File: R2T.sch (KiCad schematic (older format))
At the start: 10 parts, among them J1 12V_Input, J2 Conn_02x01, J3 Conn_01x07, J4 Conn_01x07, U0 μA78Lxx, U1 Teensy3.5

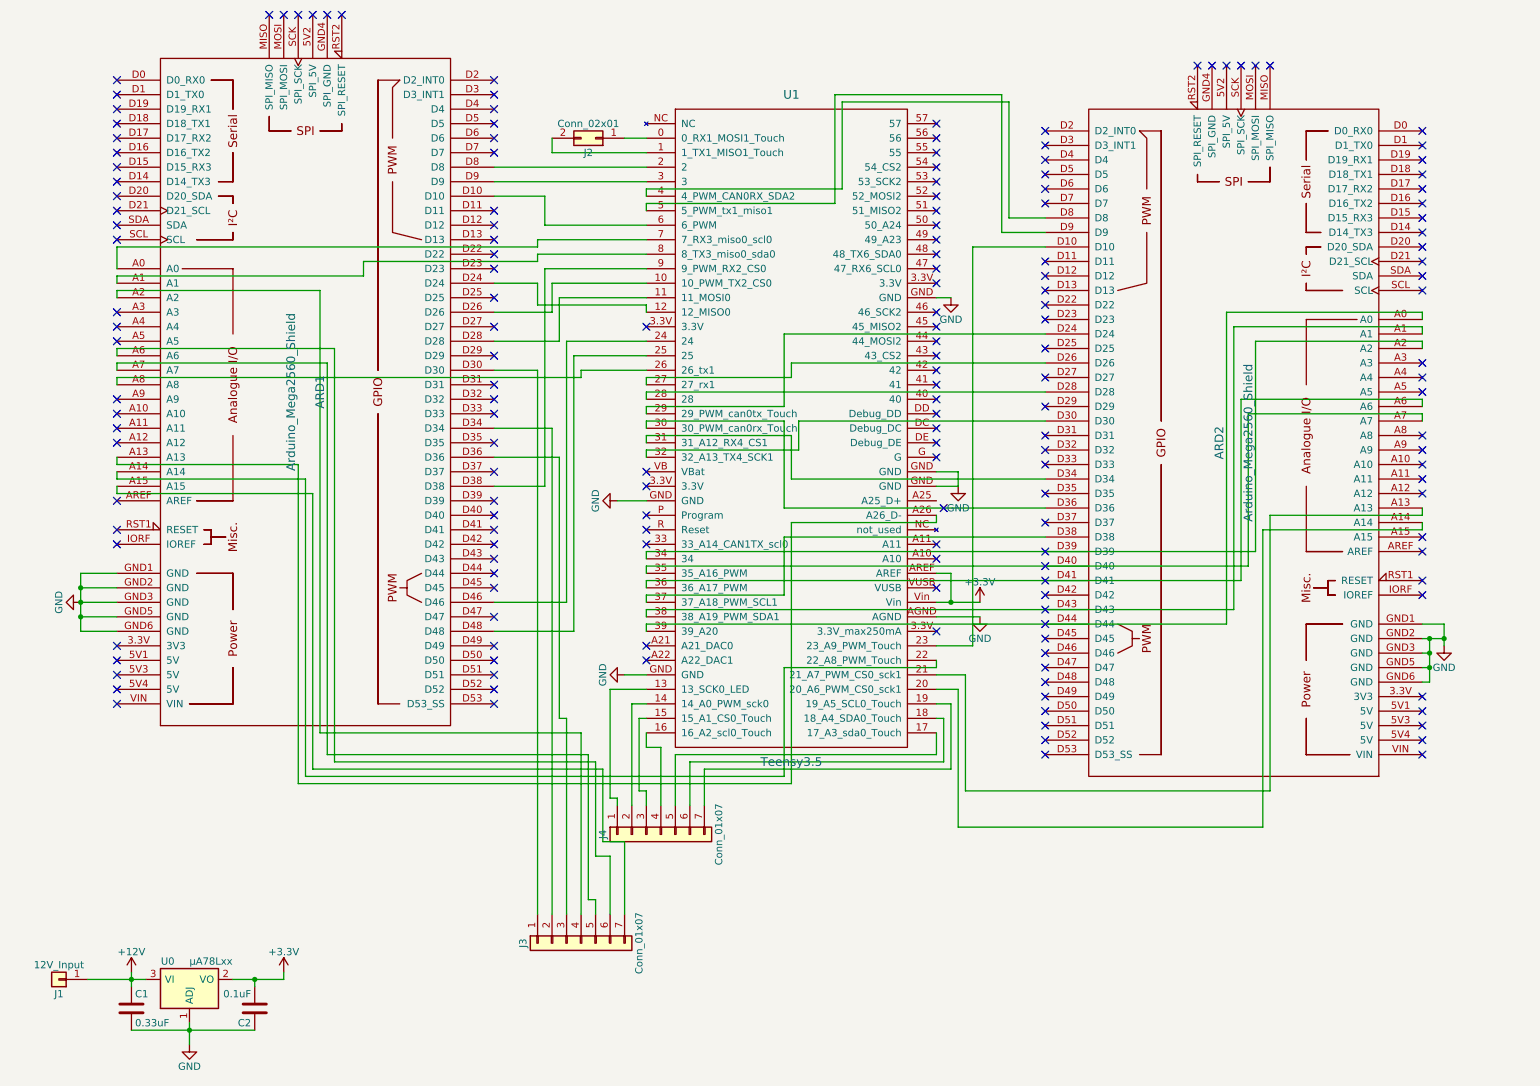
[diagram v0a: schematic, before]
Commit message: Added a 3rd pin on the connector for the serial debug on the teensy : gnd added
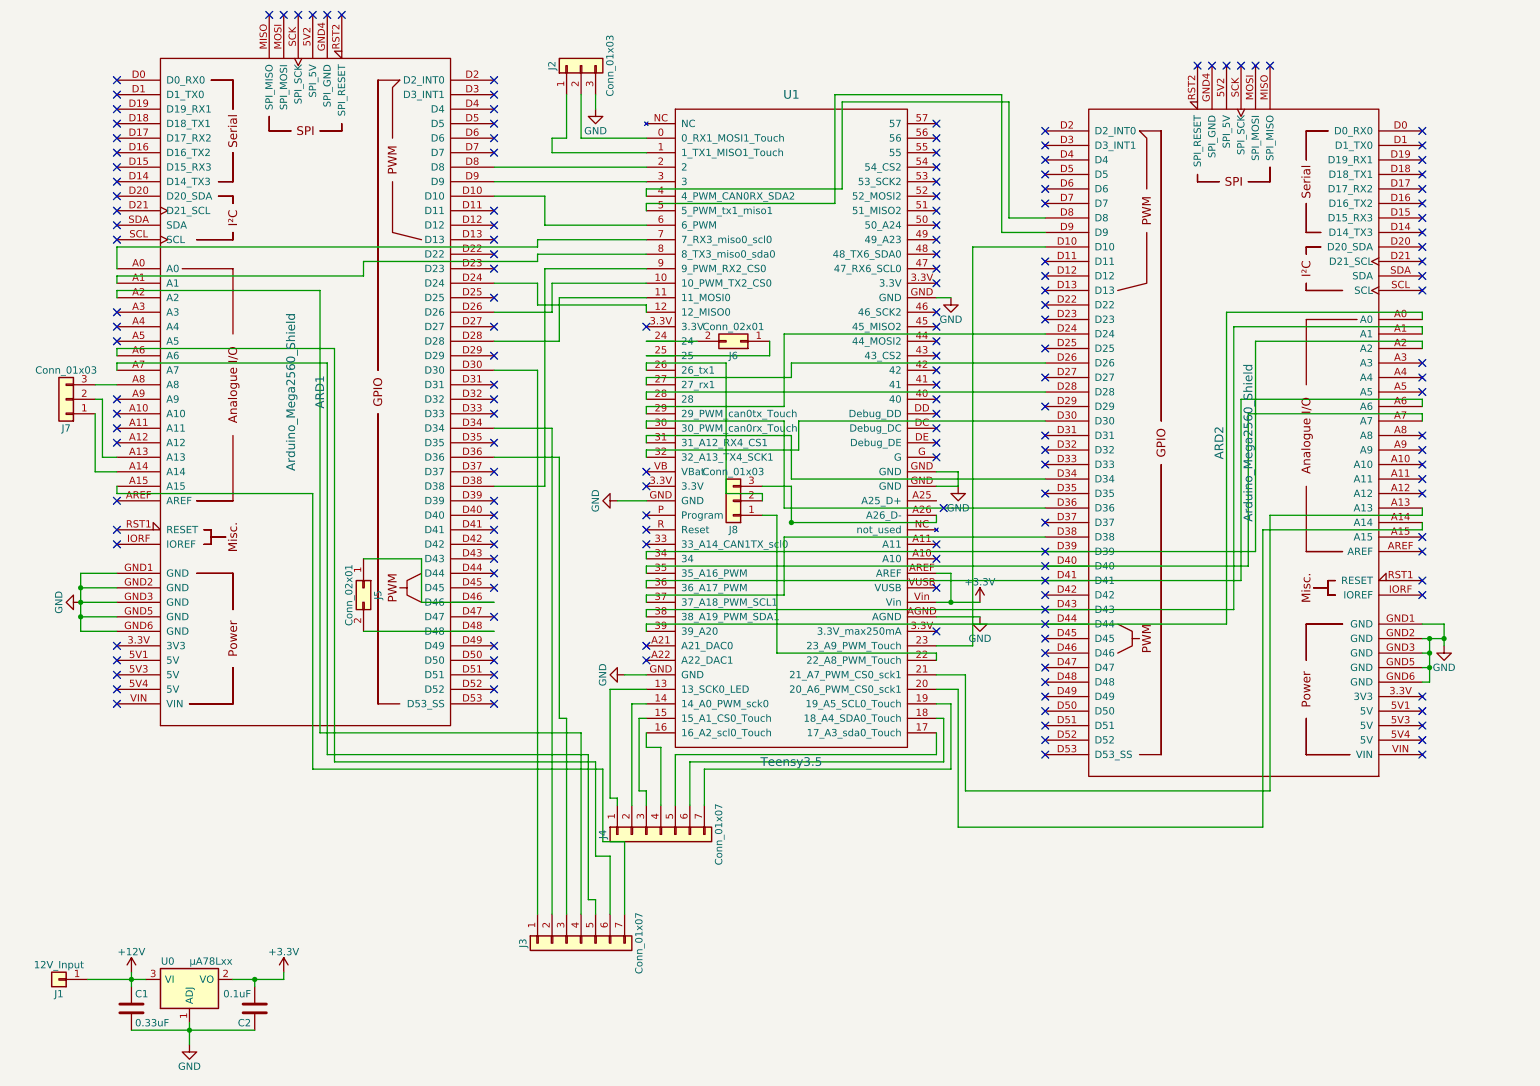
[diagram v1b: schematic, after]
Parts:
- removed J2: Conn_02x01, Connector_PinSocket_2.00mm:PinSocket_1x02_P2.00mm_Horizontal, symbol Conn_02x01
- added J2, J7, J8: Conn_01x03, Connector_PinHeader_2.00mm:PinHeader_1x03_P2.00mm_Vertical, symbol Conn_01x03
- added J5, J6: Conn_02x01, Connector_PinSocket_2.00mm:PinSocket_1x02_P2.00mm_Horizontal, symbol Conn_02x01
- J3, J4: footprint Connector_PinSocket_2.54mm:PinSocket_1x07_P2.54mm_Vertical -> Connector_PinHeader_2.00mm:PinHeader_1x07_P2.00mm_Vertical
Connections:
- net GND: now also J2.3 (Pin_3)
- net at U1.0 (0_RX1_MOSI1_Touch): now also J2.2 (Pin_2)
- net at U1.1 (1_TX1_MISO1_Touch): now also J2.1 (Pin_1)
- net at U1.22 (22_A8_PWM_Touch): now also J8.1 (Pin_1); no longer ARD1.A14
- net at U1.24: now also J6.2 (Pin_2); no longer ARD1.D46
- net at U1.25: now also J6.1 (Pin_1); no longer ARD1.D48
- net at U1.26 (26_tx1): now also J8.2 (Pin_2); no longer ARD1.A8
- net at U1.A26 (A26_D-): now also J8.3 (Pin_3); no longer ARD1.A13
- new net: ARD1.A13, J7.2 (Pin_2)
- new net: ARD1.A14, J7.1 (Pin_1)
- new net: ARD1.A8, J7.3 (Pin_3)
- new net: ARD1.D46, J5.1 (Pin_1)
- new net: ARD1.D48, J5.2 (Pin_2)
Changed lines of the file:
@@
 NoConn ~ 4750 3550
 NoConn ~ 4750 2550
-$Comp
-L Conn_02x01 J2
-U 1 1 5A55909C
-P 4400 1250
-F 0 "J2" H 4450 1350 50  0000 C CNN
-F 1 "Conn_02x01" H 4450 1150 50  0000 C CNN
-F 2 "Connector_PinSocket_2.00mm:PinSocket_1x02_P2.00mm_Horizontal" H 4400 1250 50  0001 C CNN
-F 3 "" H 4400 1250 50  0001 C CNN
-	1    4400 1250
-	-1   0    0    1
-$EndComp
 NoConn ~ 7500 4300
 NoConn ~ 7500 4200
@@
 	1100 3700 1100 3650
 Wire Wire Line
-	1100 3550 1100 3600
-Wire Wire Line
-	1100 3600 2400 3600
-Wire Wire Line
-	2400 3600 2400 5650
-Wire Wire Line
-	2400 5650 5700 5650
-Wire Wire Line
-	5700 5650 5700 4900
-Wire Wire Line
-	5700 4900 6750 4900
-Wire Wire Line
-	6750 4900 6750 4850
-Wire Wire Line
-	4750 2650 4200 2650
-Wire Wire Line
-	4200 2650 4200 4450
-Wire Wire Line
-	4200 4450 3700 4450
-Wire Wire Line
-	4750 2750 4250 2750
-Wire Wire Line
-	4250 2750 4250 4650
-Wire Wire Line
-	4250 4650 3700 4650
-Wire Wire Line
-	1100 2950 1100 2900
-Wire Wire Line
-	1100 2900 4300 2900
-Wire Wire Line
-	4300 2900 4300 2850
-Wire Wire Line
-	4300 2850 4750 2850
-Wire Wire Line
-	1100 3450 1100 3500
-Wire Wire Line
-	1100 3500 2350 3500
-Wire Wire Line
-	2350 3500 2350 5700
-Wire Wire Line
-	2350 5700 5750 5700
-Wire Wire Line
-	5750 5700 5750 3900
-Wire Wire Line
 	5750 3900 6750 3900
 Wire Wire Line
@@
 	6850 2350 6750 2350
 Wire Wire Line
-	4750 1250 4600 1250
+	4300 1250 4750 1250
 Wire Wire Line
 	4750 1350 4100 1350
@@
 F 0 "J4" H 4850 6450 50  0000 C CNN
 F 1 "Conn_01x07" H 4850 5650 50  0000 C CNN
-F 2 "Connector_PinSocket_2.54mm:PinSocket_1x07_P2.54mm_Vertical" H 4850 6050 50  0001 C CNN
+F 2 "Connector_PinHeader_2.00mm:PinHeader_1x07_P2.00mm_Vertical" H 4850 6050 50  0001 C CNN
 F 3 "" H 4850 6050 50  0001 C CNN
 	1    4850 6050
@@
 F 0 "J3" H 4300 7200 50  0000 C CNN
 F 1 "Conn_01x07" H 4300 6400 50  0000 C CNN
-F 2 "Connector_PinSocket_2.54mm:PinSocket_1x07_P2.54mm_Vertical" H 4300 6800 50  0001 C CNN
+F 2 "Connector_PinHeader_2.00mm:PinHeader_1x07_P2.00mm_Vertical" H 4300 6800 50  0001 C CNN
 F 3 "" H 4300 6800 50  0001 C CNN
 	1    4300 6800
@@
 Wire Wire Line
 	4400 6500 4400 6600
+$Comp
+L Conn_02x01 J5
+U 1 1 5A5645DD
+P 2800 4350
+F 0 "J5" H 2850 4450 50  0000 C CNN
+F 1 "Conn_02x01" H 2850 4250 50  0000 C CNN
+F 2 "Connector_PinSocket_2.00mm:PinSocket_1x02_P2.00mm_Horizontal" H 2800 4350 50  0001 C CNN
+F 3 "" H 2800 4350 50  0001 C CNN
+	1    2800 4350
+	0    1    1    0
+$EndComp
+Wire Wire Line
+	3200 4450 3200 4150
+Wire Wire Line
+	3200 4150 2800 4150
+$Comp
+L Conn_02x01 J6
+U 1 1 5A5648FB
+P 5400 2650
+F 0 "J6" H 5450 2750 50  0000 C CNN
+F 1 "Conn_02x01" H 5450 2550 50  0000 C CNN
+F 2 "Connector_PinSocket_2.00mm:PinSocket_1x02_P2.00mm_Horizontal" H 5400 2650 50  0001 C CNN
+F 3 "" H 5400 2650 50  0001 C CNN
+	1    5400 2650
+	-1   0    0    1
+$EndComp
+Wire Wire Line
+	5600 2750 5600 2650
+Wire Wire Line
+	3700 4650 2800 4650
+Wire Wire Line
+	3700 4450 3200 4450
+Wire Wire Line
+	5100 2650 4750 2650
+Wire Wire Line
+	4750 2750 5600 2750
+$Comp
+L Conn_01x03 J7
+U 1 1 5A565122
+P 750 3050
+F 0 "J7" H 750 3250 50  0000 C CNN
+F 1 "Conn_01x03" H 750 2850 50  0000 C CNN
+F 2 "Connector_PinHeader_2.00mm:PinHeader_1x03_P2.00mm_Vertical" H 750 3050 50  0001 C CNN
+F 3 "" H 750 3050 50  0001 C CNN
+	1    750  3050
+	-1   0    0    1
+$EndComp
+Wire Wire Line
+	1100 2950 950  2950
+Wire Wire Line
+	1100 3450 1000 3450
+Wire Wire Line
+	1000 3450 1000 3050
+Wire Wire Line
+	1000 3050 950  3050
+Wire Wire Line
+	950  3150 950  3550
+Wire Wire Line
+	950  3550 1100 3550
+$Comp
+L Conn_01x03 J8
+U 1 1 5A56593C
+P 5350 3750
+F 0 "J8" H 5350 3950 50  0000 C CNN
+F 1 "Conn_01x03" H 5350 3550 50  0000 C CNN
+F 2 "Connector_PinHeader_2.00mm:PinHeader_1x03_P2.00mm_Vertical" H 5350 3750 50  0001 C CNN
+F 3 "" H 5350 3750 50  0001 C CNN
+	1    5350 3750
+	-1   0    0    1
+$EndComp
+Wire Wire Line
+	6750 4800 5650 4800
+Wire Wire Line
+	5650 4800 5650 3850
+Wire Wire Line
+	5650 3850 5550 3850
+Wire Wire Line
+	5550 3750 5550 3700
+Wire Wire Line
+	5550 3700 5300 3700
+Wire Wire Line
+	5300 3700 5300 2800
+Wire Wire Line
+	5300 2800 4750 2800
+Wire Wire Line
+	4750 2800 4750 2850
+Wire Wire Line
+	5550 3650 5750 3650
+Connection ~ 5750 3900
+Wire Wire Line
+	5750 3650 5750 3900
+Wire Wire Line
+	6750 4850 6750 4800
+$Comp
+L Conn_01x03 J2
+U 1 1 5A58CBAA
+P 4300 750
+F 0 "J2" H 4300 950 50  0000 C CNN
+F 1 "Conn_01x03" H 4300 550 50  0000 C CNN
+F 2 "Connector_PinHeader_2.00mm:PinHeader_1x03_P2.00mm_Vertical" H 4300 750 50  0001 C CNN
+F 3 "" H 4300 750 50  0001 C CNN
+	1    4300 750
+	0    -1   -1   0
+$EndComp
+Wire Wire Line
+	4200 950  4200 1250
+Wire Wire Line
+	4200 1250 4100 1250
+Wire Wire Line
+	4300 950  4300 1250
+$Comp
+L GND #PWR012
+U 1 1 5A58CF2A
+P 4400 1050
+F 0 "#PWR012" H 4400 800 50  0001 C CNN
+F 1 "GND" H 4400 900 50  0000 C CNN
+F 2 "" H 4400 1050 50  0001 C CNN
+F 3 "" H 4400 1050 50  0001 C CNN
+	1    4400 1050
+	1    0    0    -1
+$EndComp
+Wire Wire Line
+	4400 950  4400 1050
 $EndSCHEMATC

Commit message: Finished seperating circuits on to 3 diffrent boards : teensy / ramps 0 / ramps 1. Sill need to clean and optimis for space and soder
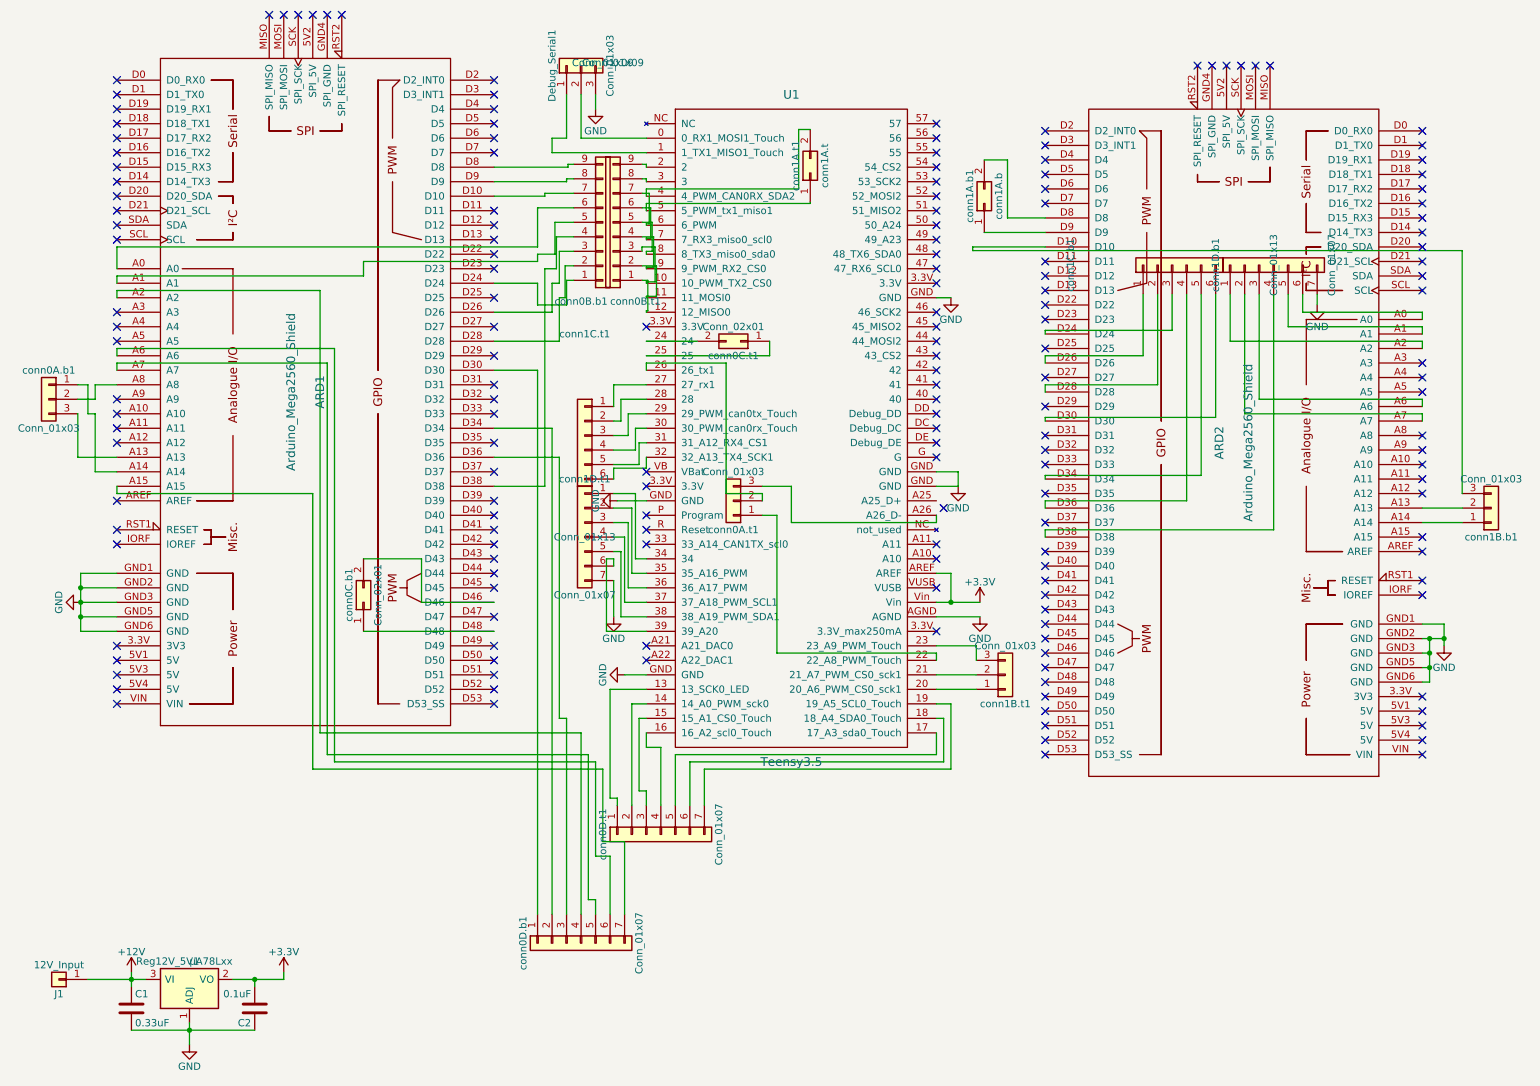
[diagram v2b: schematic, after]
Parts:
- added conn0B.b1, conn0B.t1: Conn_01x09, Connector_PinHeader_2.00mm:PinHeader_1x09_P2.00mm_Vertical, symbol Conn_01x09
- added conn1A.b1: conn1A.b, Connector_PinSocket_2.00mm:PinSocket_2x01_P2.00mm_Vertical, symbol Conn_02x01
- added conn1A.t1: conn1A.t, Connector_PinSocket_2.00mm:PinSocket_2x01_P2.00mm_Vertical, symbol Conn_02x01
- added conn1B.b1, conn1B.t1: Conn_01x03, Connector_PinSocket_2.00mm:PinSocket_1x03_P2.00mm_Vertical, symbol Conn_01x03
- added conn1C.b1, conn1C.t1: Conn_01x13, Connector_PinSocket_2.00mm:PinSocket_1x06_P2.00mm_Vertical, symbol Conn_01x06
- added conn1D.b1, conn1D.t1: Conn_01x07, Connector_PinHeader_2.00mm:PinHeader_1x07_P2.00mm_Vertical, symbol Conn_01x07
- conn0C.b1: renamed from J5; footprint Connector_PinSocket_2.00mm:PinSocket_1x02_P2.00mm_Horizontal -> Connector_PinSocket_2.00mm:PinSocket_2x01_P2.00mm_Vertical
- renumbered J2 to Debug_Serial1, U0 to Reg12V_5V1, J7 to conn0A.b1, J8 to conn0A.t1, J6 to conn0C.t1, J3 to conn0D.b1, J4 to conn0D.t1
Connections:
- net GND: now also conn1D.b1.7 (Pin_7), conn1D.t1.7 (Pin_7)
- net at U1.10 (10_PWM_TX2_CS0): now also conn0B.t1.3 (Pin_3); no longer ARD1.D26
- net at U1.11 (11_MOSI0): now also conn0B.t1.2 (Pin_2); no longer ARD1.D28
- net at U1.12 (12_MISO0): now also conn0B.t1.1 (Pin_1); no longer ARD1.D24
- net at U1.2: now also conn0B.t1.9 (Pin_9); no longer ARD1.D8
- net at U1.20 (20_A6_PWM_CS0_sck1): now also conn1B.t1.1 (Pin_1); no longer ARD2.A14
- net at U1.21 (21_A7_PWM_CS0_sck1): now also conn1B.t1.2 (Pin_2); no longer ARD2.A13
- net at U1.23 (23_A9_PWM_Touch): now also conn1B.t1.3 (Pin_3); no longer ARD2.D10
- net at U1.27 (27_rx1): now also conn1C.t1.1 (Pin_1); no longer ARD2.D26
- net at U1.28: now also conn1C.t1.2 (Pin_2); no longer ARD2.D28
- net at U1.29 (29_PWM_can0tx_Touch): now also conn1C.t1.3 (Pin_3); no longer ARD2.D24
- net at U1.3: now also conn0B.t1.8 (Pin_8); no longer ARD1.D9
- net at U1.30 (30_PWM_can0rx_Touch): now also conn1C.t1.4 (Pin_4); no longer ARD2.D36
- net at U1.31 (31_A12_RX4_CS1): now also conn1C.t1.5 (Pin_5); no longer ARD2.D34
- net at U1.32 (32_A13_TX4_SCK1): now also conn1C.t1.6 (Pin_6); no longer ARD2.D30
- net at U1.34: now also conn1D.t1.1 (Pin_1); no longer ARD2.A2
- net at U1.35 (35_A16_PWM): now also conn1D.t1.2 (Pin_2); no longer ARD2.A7
- net at U1.36 (36_A17_PWM): now also conn1D.t1.3 (Pin_3); no longer ARD2.A6
- net at U1.37 (37_A18_PWM_SCL1): now also conn1D.t1.4 (Pin_4); no longer ARD2.D38
- net at U1.38 (38_A19_PWM_SDA1): now also conn1D.t1.5 (Pin_5); no longer ARD2.A1
- net at U1.39 (39_A20): now also conn1D.t1.6 (Pin_6); no longer ARD2.A0
- net at U1.4 (4_PWM_CAN0RX_SDA2): now also conn1A.t1.2 (Pin_2); no longer ARD2.D8
- net at U1.5 (5_PWM_tx1_miso1): now also conn1A.t1.1 (Pin_1); no longer ARD2.D9
- net at U1.6 (6_PWM): now also conn0B.t1.7 (Pin_7); no longer ARD1.D10
- net at U1.7 (7_RX3_miso0_scl0): now also conn0B.t1.6 (Pin_6); no longer ARD1.A0
- net at U1.8 (8_TX3_miso0_sda0): now also conn0B.t1.5 (Pin_5); no longer ARD1.A1
- net at U1.9 (9_PWM_RX2_CS0): now also conn0B.t1.4 (Pin_4); no longer ARD1.D38
- net at ARD1.A13: now also conn0A.b1.3 (Pin_3); no longer conn0A.b1.2 (Pin_2)
- net at ARD1.A8: now also conn0A.b1.2 (Pin_2); no longer conn0A.b1.3 (Pin_3)
- net at ARD1.D46: now also conn0C.b1.2 (Pin_2); no longer conn0C.b1.1 (Pin_1)
- net at ARD1.D48: now also conn0C.b1.1 (Pin_1); no longer conn0C.b1.2 (Pin_2)
- new net: ARD1.A0, conn0B.b1.6 (Pin_6)
- new net: ARD1.A1, conn0B.b1.5 (Pin_5)
- new net: ARD1.D10, conn0B.b1.7 (Pin_7)
- new net: ARD1.D24, conn0B.b1.1 (Pin_1)
- new net: ARD1.D26, conn0B.b1.3 (Pin_3)
- new net: ARD1.D28, conn0B.b1.2 (Pin_2)
- new net: ARD1.D38, conn0B.b1.4 (Pin_4)
- new net: ARD1.D8, conn0B.b1.9 (Pin_9)
- new net: ARD1.D9, conn0B.b1.8 (Pin_8)
- new net: ARD2.A0, conn1D.b1.6 (Pin_6)
- new net: ARD2.A1, conn1D.b1.5 (Pin_5)
- new net: ARD2.A13, conn1B.b1.2 (Pin_2)
- new net: ARD2.A14, conn1B.b1.1 (Pin_1)
- new net: ARD2.A2, conn1D.b1.1 (Pin_1)
- new net: ARD2.A6, conn1D.b1.3 (Pin_3)
- new net: ARD2.A7, conn1D.b1.2 (Pin_2)
- new net: ARD2.D10, conn1B.b1.3 (Pin_3)
- new net: ARD2.D24, conn1C.b1.3 (Pin_3)
- new net: ARD2.D26, conn1C.b1.1 (Pin_1)
- new net: ARD2.D28, conn1C.b1.2 (Pin_2)
- new net: ARD2.D30, conn1C.b1.6 (Pin_6)
- new net: ARD2.D34, conn1C.b1.5 (Pin_5)
- new net: ARD2.D36, conn1C.b1.4 (Pin_4)
- new net: ARD2.D38, conn1D.b1.4 (Pin_4)
- new net: ARD2.D8, conn1A.b1.2 (Pin_2)
- new net: ARD2.D9, conn1A.b1.1 (Pin_1)
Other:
- moved on the sheet: conn0A.b1

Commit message: Finished cleaning
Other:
- moved on the sheet: conn0B.b1
